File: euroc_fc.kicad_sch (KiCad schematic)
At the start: 143 parts, among them J1 Micro-Fit, J10 USB_C_Receptacle_USB2.0, J11 SWD Header, J2 Micro-Fit, J3 Micro-Fit, J4 SMA, J5 JST-GH, J6 JST-GH, J7 JST-GH, J8 JST-GH, J9 Micro_SD_Card_Det, Q1 DMN2056U, Q2 AOSP21321, Q3 DMN2056U, Q4 AOSP21321, Q5 DMN2056U, Q6 DMN2056U, Q7 DMN2056U, SW1 EVQ-PUC02K, SW2 EVQ-PUC02K, U1 STM32F401RCT6, U10 Ai-Thinker-Ra-01, U11 W25Q256JVF, U2 L7805, U3 L7805, U4 AZ1117I-3.3, U5 LSM6DSR, U6 ADXL375, U7 MS5611-01BA, U8 BMM150, U9 SAM-M8Q, Y1 25M

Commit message: Restructure BOM
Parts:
- BZ1: DigiKey# (none) -> 102-CMT-8504-100-SMT-CT-ND; Manufacturer (none) -> CUI Devices; Part# (none) -> CMT-8504-100-SMT-TR; Vendor https://www.digikey.de/de/products/detail/cui-devices/CMT-8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 -> (none)
- C1, C11, C2, C3, C4, C5: LCSC# (none) -> C12891; Manufacturer (none) -> Samsung Electro-Mechanics; Part# (none) -> CL31A226KAHNNNE; Vendor https://www.lcsc.com/product-detail/Multilayer-Ceramic-Capa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 -> (none)
- C10, C36: LCSC# (none) -> C14860; Manufacturer (none) -> Samsung Electro-Mechanics; Part# (none) -> CL31B106KAHNNNE; Vendor https://www.lcsc.com/product-detail/Multilayer-Ceramic-Capa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 -> (none)
- C12: LCSC# (none) -> C1872; Manufacturer (none) -> Samsung Electro-Mechanics; Part# (none) -> CL31B475KAHNNNE; Vendor https://www.lcsc.com/product-detail/Multilayer-Ceramic-Capa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 -> (none)
- C13, C14, C15, C16, C17, C19, C24, C25, C27, C28, C29, C30, C31, C32, C33, C37, C38, C39, C7, C9: LCSC# (none) -> C1591; Manufacturer (none) -> Samsung Electro-Mechanics; Part# (none) -> CL10B104KB8NNNC; Vendor https://www.lcsc.com/product-detail/Multilayer-Ceramic-Capa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 -> (none)
- C18, C26: LCSC# (none) -> C318694; Manufacturer (none) -> Samsung Electro-Mechanics; Part# (none) -> CL21A105KBCLNNC; Vendor https://www.lcsc.com/product-detail/Multilayer-Ceramic-Capa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 -> (none)
- C20, C23: LCSC# (none) -> C377773; Manufacturer (none) -> Samsung Electro-Mechanics; Part# (none) -> CL21A225KBQNNNE; Vendor https://www.lcsc.com/product-detail/Multilayer-Ceramic-Capa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 -> (none)
- C21, C22: LCSC# (none) -> C1653; Manufacturer (none) -> Samsung Electro-Mechanics; Part# (none) -> CL10C220JB8NNNC; Vendor https://www.lcsc.com/product-detail/Multilayer-Ceramic-Capa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 -> (none)
- C34, C35, F3, F4, F5, F6, H1, H2, H3, H4, H5, H6, JP1, JP2, JP3, JP4, TP1, TP10, TP11, TP12, TP13, TP14, TP15, TP16, TP17, TP18, TP19, TP2, TP20, TP21, TP3, TP4, TP5, TP6, TP7, TP8, TP9: DigiKey# (none) -> N/A; LCSC# (none) -> N/A; Manufacturer (none) -> N/A; Part# (none) -> N/A; Vendor N/A -> (none)
- C6, C8: LCSC# (none) -> C159798; Manufacturer (none) -> Samsung Electro-Mechanics; Part# (none) -> CL10B334KO8NNNC; Vendor https://www.lcsc.com/product-detail/Multilayer-Ceramic-Capa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 -> (none)
- D1, D2, D3, D9: DigiKey# (none) -> SS26FLCT-ND; Manufacturer (none) -> onsemi; Part# (none) -> SS26FL; Vendor https://www.digikey.de/de/products/detail/onsemi/SS26FL/530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 -> (none)
- D4, D5, D6: DigiKey# (none) -> 475-2512-1-ND; Manufacturer (none) -> OSRAM Opto Semiconductors Inc.; Part# (none) -> LS Q976-NR-1; Vendor https://www.digikey.de/de/products/detail/osram-opto-semico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 -> (none)
- D7: DigiKey# (none) -> 475-2486-1-ND; Manufacturer (none) -> OSRAM Opto Semiconductors Inc.; Part# (none) -> LO Q976-PS-25-0-20-R18; Vendor https://www.digikey.de/de/products/detail/osram-opto-semico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 -> (none)
- D8: DigiKey# (none) -> 475-3754-1-ND; Manufacturer (none) -> OSRAM Opto Semiconductors Inc.; Part# (none) -> LG Q396-PS-35; Vendor https://www.digikey.de/de/products/detail/osram-opto-semico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 -> (none)
- F1, F2: DigiKey# (none) -> 507-1942-1-ND; Manufacturer (none) -> Bel Fuse Inc.; Part# (none) -> 0685H9100-01; Vendor https://www.digikey.de/de/products/detail/bel-fuse-inc/0685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 -> (none)
- J1, J2, J3: LCSC# (none) -> C122413; Manufacturer (none) -> MOLEX; Part# (none) -> 0430450400; Vendor https://www.lcsc.com/product-detail/Wire-To-Board-Wire-To-W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 -> (none)
- J10: DigiKey# (none) -> 12401610E4#2ACT-ND; Manufacturer (none) -> Amphenol CS; Part# (none) -> 12401610E4#2A; Vendor https://www.digikey.de/de/products/detail/amphenol-icc-comm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 -> (none)
- J4: DigiKey# (none) -> 17-2016504-1-ND; Manufacturer (none) -> TE Connectivity AMP Connectors; Part# (none) -> 2016504-1; Vendor https://www.digikey.de/de/products/detail/te-connectivity-a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 -> (none)
- J9: LCSC# (none) -> C114218; Manufacturer (none) -> Hirose; Part# (none) -> DM3AT-SF-PEJM5; Vendor https://www.lcsc.com/product-detail/SD-Card-Connectors_HRS-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 -> (none)
- L1, L2, L3: LCSC# (none) -> C19330; Manufacturer (none) -> Murata Electronics; Part# (none) -> BLM18AG601SN1D; Vendor https://www.lcsc.com/product-detail/Ferrite-Beads_Murata-El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 -> (none)
- Q1, Q3, Q5, Q6, Q7: LCSC# (none) -> C332302; Manufacturer (none) -> Diodes Incorporated; Part# (none) -> DMN2056U-7; Vendor https://www.lcsc.com/product-detail/MOSFETs_Diodes-Incorpor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 -> (none)
- Q2, Q4: LCSC# (none) -> C560863; Manufacturer (none) -> Alpha & Omega Semicon; Part# (none) -> AOSP21321; Vendor https://www.lcsc.com/product-detail/MOSFETs_Alpha-Omega-Sem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 -> (none)
- R1: LCSC# (none) -> C375688; Manufacturer (none) -> YAGEO; Part# (none) -> PA2512FKE7W0R01E; Vendor https://www.lcsc.com/product-detail/Current-Sense-Resistors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 -> (none)
- R10, R12, R14: LCSC# (none) -> C185354; Manufacturer (none) -> YAGEO; Part# (none) -> RC0603FR-071K8L; Vendor https://www.lcsc.com/product-detail/Chip-Resistor-Surface-M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 -> (none)
- R11, R13, R15, R21, R22: LCSC# (none) -> C22548; Manufacturer (none) -> YAGEO; Part# (none) -> RC0603FR-071KL; Vendor https://www.lcsc.com/product-detail/Chip-Resistor-Surface-M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 -> (none)
- R16, R17: LCSC# (none) -> C107701; Manufacturer (none) -> YAGEO; Part# (none) -> RC0603FR-0722RL; Vendor https://www.lcsc.com/product-detail/Chip-Resistor-Surface-M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 -> (none)
- R18, R19: LCSC# (none) -> C105580; Manufacturer (none) -> YAGEO; Part# (none) -> RC0603FR-075K1L; Vendor https://www.lcsc.com/product-detail/Chip-Resistor-Surface-M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 -> (none)
- R2, R3, R7, R8, R9: LCSC# (none) -> C2085669; Manufacturer (none) -> ROHM Semicon; Part# (none) -> ESR03EZPJ221; Vendor https://www.lcsc.com/product-detail/Chip-Resistor-Surface-M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 -> (none)
- R20: LCSC# (none) -> C100044; Manufacturer (none) -> YAGEO; Part# (none) -> RC0603FR-070RL; Vendor https://www.lcsc.com/product-detail/Chip-Resistor-Surface-M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 -> (none)
- R4, R6: LCSC# (none) -> C98220; Manufacturer (none) -> YAGEO; Part# (none) -> RC0603FR-0710KL; Vendor https://www.lcsc.com/product-detail/Chip-Resistor-Surface-M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 -> (none)
- R5: LCSC# (none) -> C105881; Manufacturer (none) -> YAGEO; Part# (none) -> RC0603FR-07330RL; Vendor https://www.lcsc.com/product-detail/Chip-Resistor-Surface-M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 -> (none)
- SW1, SW2: LCSC# (none) -> C79174; Manufacturer (none) -> Panasonic; Part# (none) -> EVQPUC02K; Vendor https://www.lcsc.com/product-detail/Tactile-Switches_PANASO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 -> (none)
- U1: LCSC# (none) -> C74524; Manufacturer (none) -> STMicroelectronics; Part# (none) -> STM32F401RCT6; Vendor https://www.lcsc.com/product-detail/ST-Microelectronics_STM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 -> (none)
- U10: LCSC# (none) -> C2830749; Manufacturer (none) -> Ai-Thinker; Part# (none) -> Ra-01SC; Vendor https://www.lcsc.com/product-detail/LoRa-Modules_Ai-Thinker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 -> (none)
- U11: DigiKey# (none) -> W25Q256JVFIQ-ND; Manufacturer (none) -> Winbond Electronics; Part# (none) -> W25Q256JVFIQ; Vendor https://www.digikey.de/en/products/detail/winbond-electroni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 -> (none)
- U2, U3: LCSC# (none) -> C310413; Manufacturer (none) -> STMicroelectronics; Part# (none) -> L7805CDT-TR; Vendor https://www.lcsc.com/product-detail/Linear-Voltage-Regulato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 -> (none)
- U4: LCSC# (none) -> C92102; Manufacturer (none) -> Diodes Incorporated; Part# (none) -> AZ1117CH-3.3TRG1; Vendor https://www.digikey.de/de/products/detail/diodes-incorporat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 -> (none)
- U5: LCSC# (none) -> C784817; Manufacturer (none) -> STMicroelectronics; Part# (none) -> LSM6DSRTR; Vendor https://www.lcsc.com/product-detail/Motion-Sensors-Accelero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 -> (none)
- U6: DigiKey# (none) -> 505-ADXL375BCCZ-ND; Manufacturer (none) -> Analog Devices Inc.; Part# (none) -> ADXL375BCCZ; Vendor https://www.digikey.de/de/products/detail/analog-devices-in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 -> (none)
- U7: DigiKey# (none) -> 223-1622-1-ND; Manufacturer (none) -> TE Connectivity Measurement Specialties; Part# (none) -> MS561101BA03-50; Vendor https://www.digikey.de/de/products/detail/te-connectivity-m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 -> (none)
- U8: LCSC# (none) -> C171681; Manufacturer (none) -> Bosch Sensortec; Part# (none) -> BMM150; Vendor https://www.lcsc.com/product-detail/Magnetic-Sensors_Bosch-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 -> (none)
- U9: DigiKey# (none) -> 672-1054-1-ND; Manufacturer (none) -> U-Blox; Part# (none) -> SAM-M8Q-0-10; Vendor https://www.digikey.de/de/products/detail/u-blox/SAM-M8Q-0-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 -> (none)
- Y1: DigiKey# (none) -> 535-9140-1-ND; Manufacturer (none) -> Abracon LLC; Part# (none) -> ABM8-25.000MHZ-B2-T; Vendor https://www.digikey.de/de/products/detail/abracon-llc/ABM8-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 -> (none)

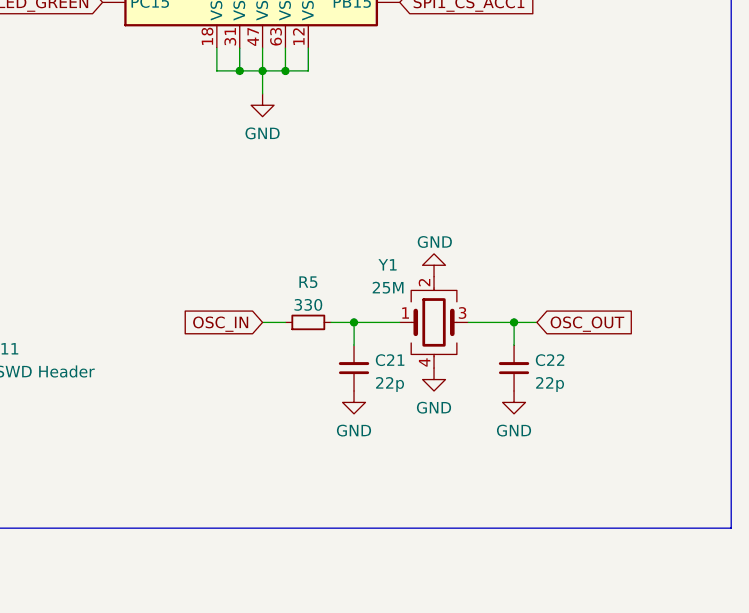
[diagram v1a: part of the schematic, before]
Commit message: Replace crystal oscillator part
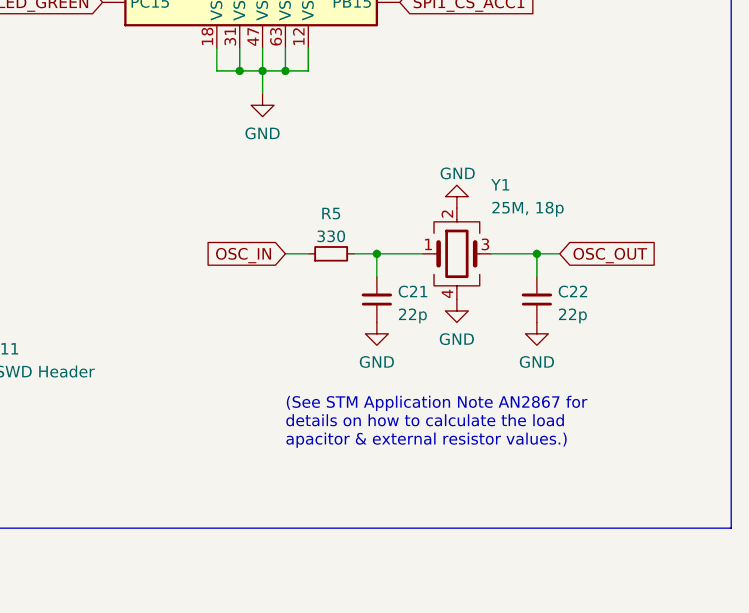
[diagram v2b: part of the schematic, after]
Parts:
- Y1: value 25M -> 25M, 18p; footprint Crystal:Crystal_SMD_Abracon_ABM8G-4Pin_3.2x2.5mm -> Oscillator:Oscillator_SMD_SeikoEpson_SG210-4Pin_2.5x2.0mm; DigiKey# 535-9140-1-ND -> (none); LCSC# (none) -> C255956; Manufacturer Abracon LLC -> Seiko Epson; Part# ABM8-25.000MHZ-B2-T -> Q24FA20H0039000
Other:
- note added: "(See STM Application Note AN2867 for details on how to calculate the load apacitor & external resistor values.)"
- moved on the sheet: C21, C22, R5, Y1

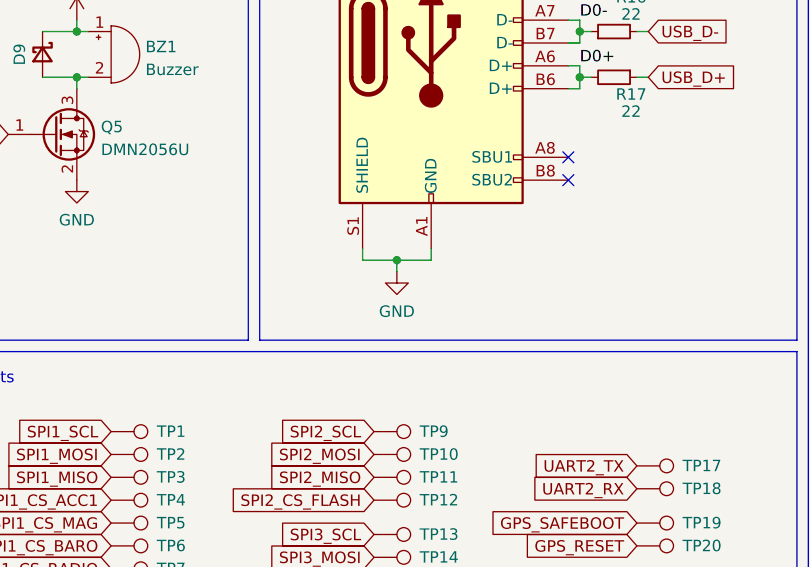
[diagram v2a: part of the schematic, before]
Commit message: Replace USB connector
New part is cheaper, smaller, easier to solder and avilable at LCSC.
Also, don't ground the USB shield anymore.
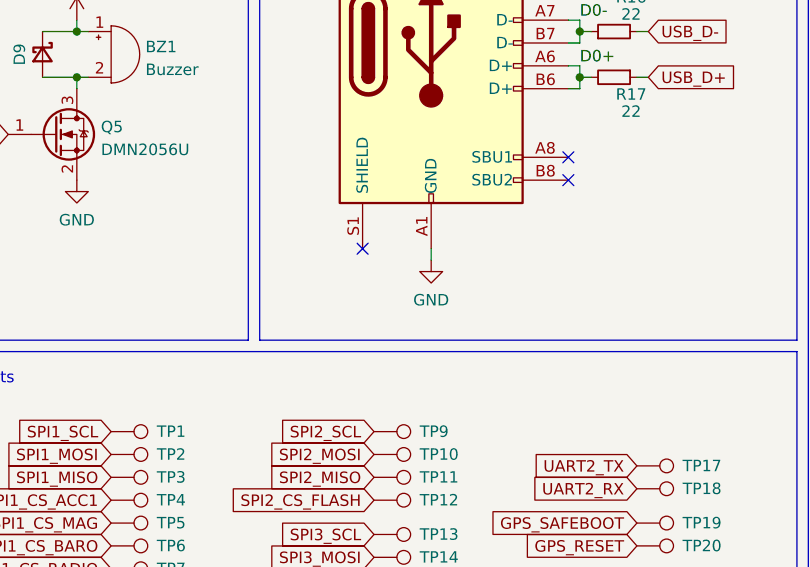
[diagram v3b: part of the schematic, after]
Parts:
- J10: footprint Connector_USB:USB_C_Receptacle_Amphenol_12401610E4-2A -> Connector_USB:USB_C_Receptacle_Palconn_UTC16-G; DigiKey# 12401610E4#2ACT-ND -> (none); LCSC# (none) -> C709357; Manufacturer Amphenol CS -> Shenzhen Kinghelm Elec; Part# 12401610E4#2A -> KH-TYPE-C-16P
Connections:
- net GND: no longer J10.S1 (SHIELD)
- no-connect marks 30 -> 31
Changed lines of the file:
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@@
   (junction (at 273.05 109.22) (diameter 0) (color 0 0 0 0)
   )
-  (junction (at 254 181.61) (diameter 0) (color 0 0 0 0)
-  )
   (junction (at 392.43 29.21) (diameter 0) (color 0 0 0 0)
   )
@@
   (no_connect (at 210.82 269.24))
   (no_connect (at 210.82 266.7))
+  (no_connect (at 250.19 180.34))
   (no_connect (at 53.34 261.62))
   (no_connect (at 96.52 30.48))
@@
     (stroke (width 0) (type default) (color 0 0 0 0))
   )
-  (wire (pts (xy 257.81 180.34) (xy 257.81 181.61))
-    (stroke (width 0) (type default) (color 0 0 0 0))
-  )
   (wire (pts (xy 260.35 100.33) (xy 260.35 102.87))
     (stroke (width 0) (type default) (color 0 0 0 0))
@@
     (stroke (width 0) (type default) (color 0 0 0 0))
   )
-  (wire (pts (xy 250.19 181.61) (xy 254 181.61))
-    (stroke (width 0) (type default) (color 0 0 0 0))
-  )
   (polyline (pts (xy 252.73 13.97) (xy 252.73 85.09))
     (stroke (width 0) (type default) (color 0 0 0 0))
@@
     (stroke (width 0) (type default) (color 0 0 0 0))
   )
-  (wire (pts (xy 250.19 180.34) (xy 250.19 181.61))
-    (stroke (width 0) (type default) (color 0 0 0 0))
-  )
   (wire (pts (xy 150.495 24.13) (xy 150.495 22.86))
     (stroke (width 0) (type default) (color 0 0 0 0))
@@
     (stroke (width 0) (type default) (color 0 0 0 0))
   )
-  (wire (pts (xy 254 181.61) (xy 254 182.88))
+  (wire (pts (xy 257.81 180.34) (xy 257.81 181.61))
     (stroke (width 0) (type default) (color 0 0 0 0))
   )
@@
     (stroke (width 0) (type default) (color 0 0 0 0))
   )
-  (wire (pts (xy 257.81 181.61) (xy 254 181.61))
-    (stroke (width 0) (type default) (color 0 0 0 0))
-  )
   (wire (pts (xy 24.13 91.44) (xy 24.13 90.17))
     (stroke (width 0) (type default) (color 0 0 0 0))
@@
     (property "Reference" "J10" (id 0) (at 257.81 136.0002 0))
     (property "Value" "USB_C_Receptacle_USB2.0" (id 1) (at 257.81 138.5371 0))
-    (property "Footprint" "Connector_USB:USB_C_Receptacle_Amphenol_12401610E4-2A" (id 2) (at 261.62 157.48 0)
+    (property "Footprint" "Connector_USB:USB_C_Receptacle_Palconn_UTC16-G" (id 2) (at 261.62 157.48 0)
+      (effects (font (size 1.27 1.27)) hide)
+    )
+    (property "Datasheet" "https://datasheet.lcsc.com/lcsc/2009111434_Shenzhen-Kinghelm-Elec-KH-TYPE-C-16P_C709357.pdf" (id 3) (at 261.62 157.48 0)
       (effects (font (size 1.27 1.27)) hide)
     )
-    (property "Datasheet" "https://www.amphenol-cs.com/media/wysiwyg/files/drawing/12401610e4x2a.pdf" (id 3) (at 261.62 157.48 0)
+    (property "DigiKey#" "" (id 5) (at 257.81 157.48 0)
       (effects (font (size 1.27 1.27)) hide)
     )
-    (property "DigiKey#" "12401610E4#2ACT-ND" (id 5) (at 257.81 157.48 0)
+    (property "Manufacturer" "Shenzhen Kinghelm Elec" (id 6) (at 257.81 157.48 0)
       (effects (font (size 1.27 1.27)) hide)
     )
-    (property "Manufacturer" "Amphenol CS" (id 6) (at 257.81 157.48 0)
+    (property "Part#" "KH-TYPE-C-16P " (id 7) (at 257.81 157.48 0)
       (effects (font (size 1.27 1.27)) hide)
     )
-    (property "Part#" "12401610E4#2A" (id 7) (at 257.81 157.48 0)
+    (property "LCSC#" "C709357" (id 8) (at 257.81 157.48 0)
       (effects (font (size 1.27 1.27)) hide)
     )
@@
     (pin "1")
   )
-  (symbol (lib_id "power:GND") (at 254 182.88 0) (unit 1)
+  (symbol (lib_id "power:GND") (at 257.81 181.61 0) (unit 1)
     (in_bom yes) (on_board yes) (fields_autoplaced)
-    (property "Reference" "#PWR0147" (id 0) (at 254 189.23 0)
+    (property "Reference" "#PWR0147" (id 0) (at 257.81 187.96 0)
       (effects (font (size 1.27 1.27)) hide)
     )
-    (property "Value" "GND" (id 1) (at 254 187.3234 0))
-    (property "Footprint" "" (id 2) (at 254 182.88 0)
+    (property "Value" "GND" (id 1) (at 257.81 186.0534 0))
+    (property "Footprint" "" (id 2) (at 257.81 181.61 0)
       (effects (font (size 1.27 1.27)) hide)
     )
-    (property "Datasheet" "" (id 3) (at 254 182.88 0)
+    (property "Datasheet" "" (id 3) (at 257.81 181.61 0)
       (effects (font (size 1.27 1.27)) hide)
     )
@@
     )
     (path "/9e4b8ac2-b588-40c5-8bdb-b7ecde2eb3b8"
-      (reference "J10") (unit 1) (value "USB_C_Receptacle_USB2.0") (footprint "Connector_USB:USB_C_Receptacle_Amphenol_12401610E4-2A")
+      (reference "J10") (unit 1) (value "USB_C_Receptacle_USB2.0") (footprint "Connector_USB:USB_C_Receptacle_Palconn_UTC16-G")
     )
     (path "/b768f538-1872-4704-96af-f7fe1fe80548"

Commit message: Substitute various parts with LCSC alternatives
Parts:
- BZ1: LCSC# (none) -> C781886; Notes (none) -> (or YUEXIN YX-SMD8530P from LCSC)
- D1, D2, D3, D9: value SS26FL -> ~; DigiKey# SS26FLCT-ND -> (none); LCSC# (none) -> C167645; Manufacturer onsemi -> Nexperia; Part# SS26FL -> PMEG3020EH,115
- D4, D5, D6: DigiKey# 475-2512-1-ND -> (none); LCSC# (none) -> C474026; Manufacturer OSRAM Opto Semiconductors Inc. -> Everlight Elec; Part# LS Q976-NR-1 -> 19-213/RSC-BS2T2B/3T
- D7: DigiKey# 475-2486-1-ND -> (none); LCSC# (none) -> C72038; Manufacturer OSRAM Opto Semiconductors Inc. -> Everlight Elec; Part# LO Q976-PS-25-0-20-R18 -> 19-213/Y2C-CQ2R2L/3T(CY)
- D8: DigiKey# 475-3754-1-ND -> (none); LCSC# (none) -> C72043; Manufacturer OSRAM Opto Semiconductors Inc. -> Everlight Elec; Part# LG Q396-PS-35 -> 19-217/GHC-YR1S2/3T
- F1, F2: DigiKey# 507-1942-1-ND -> (none); LCSC# (none) -> C207003; Manufacturer Bel Fuse Inc. -> Littelfuse; Part# 0685H9100-01 -> 0501010.WR1
- J4: DigiKey# 17-2016504-1-ND -> (none); LCSC# (none) -> C411575; Manufacturer TE Connectivity AMP Connectors -> Shenzhen Kinghelm Elec; Part# 2016504-1 -> KH-SMA-K513-G
